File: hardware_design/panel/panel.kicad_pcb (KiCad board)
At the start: 2 copper layers, 60.6 x 128.5 mm, 19 parts

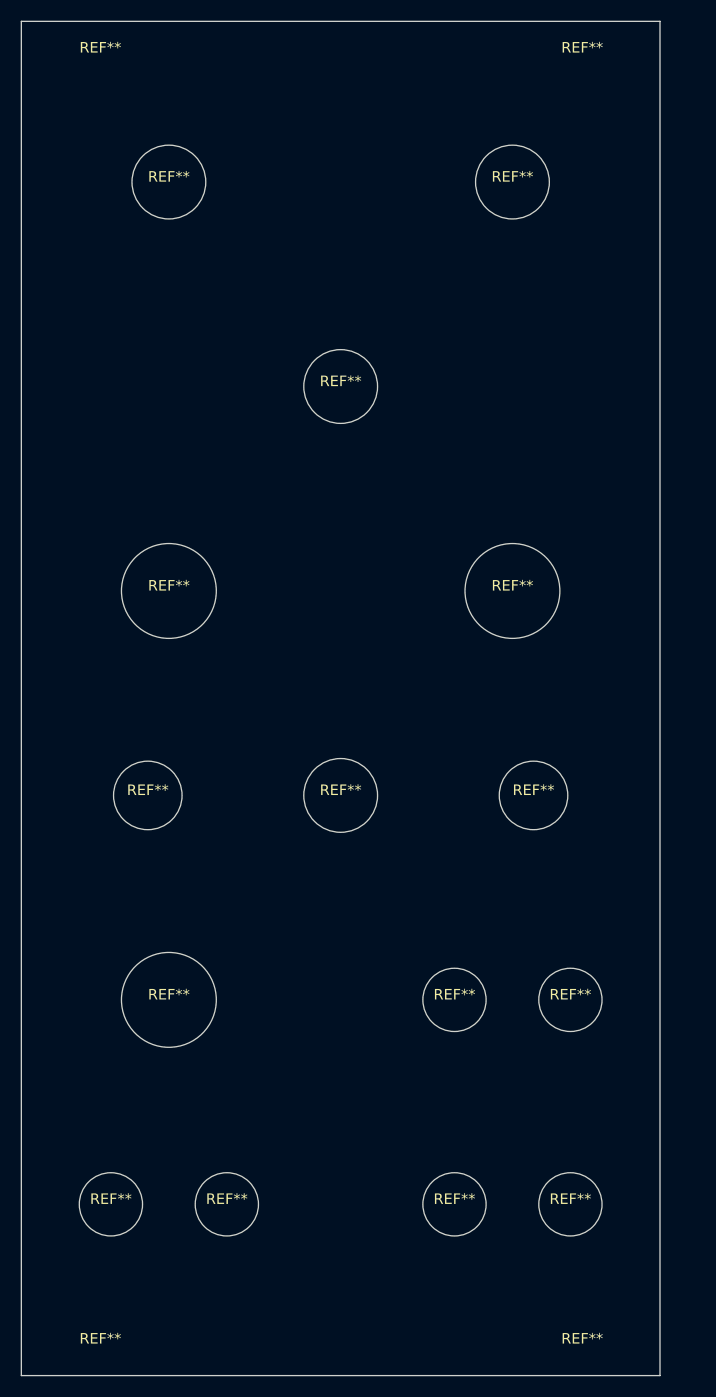
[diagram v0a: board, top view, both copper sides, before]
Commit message: Software switch de-bounce added as a result of Rev 2 testing.
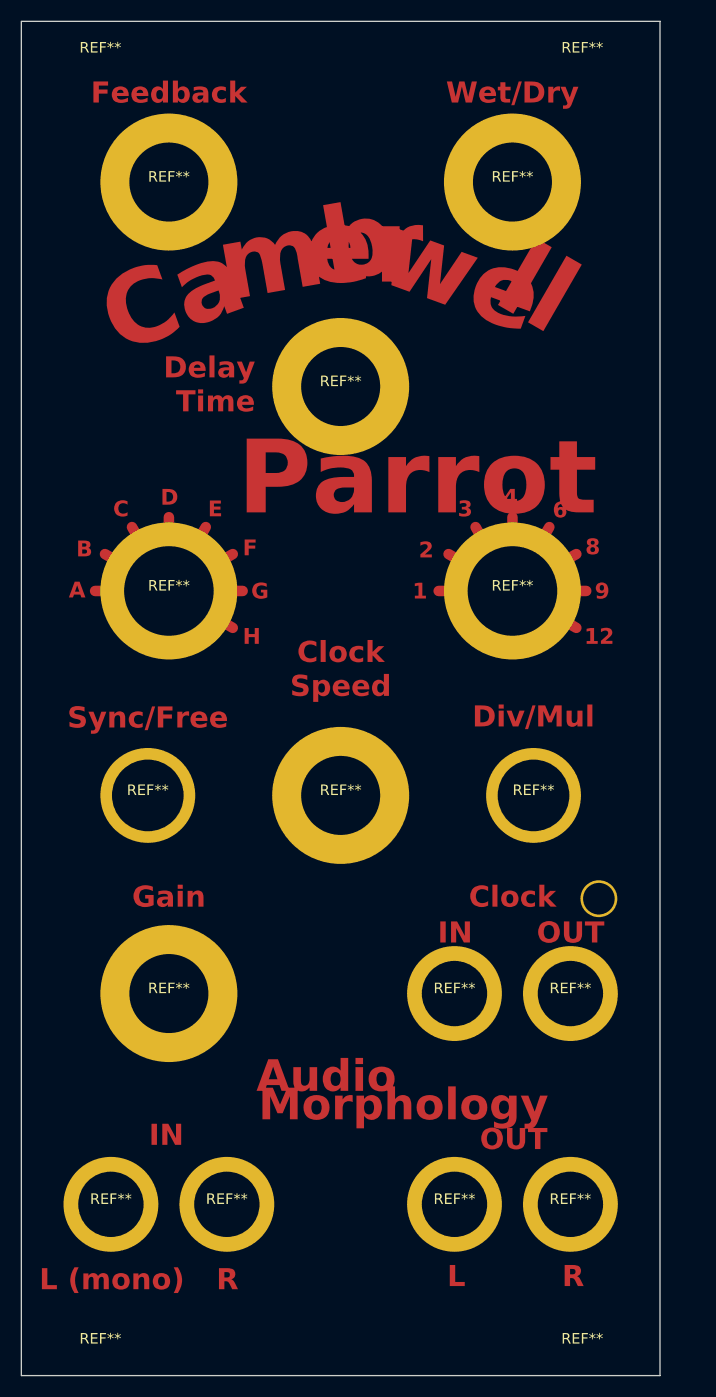
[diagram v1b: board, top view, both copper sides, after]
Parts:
- removed the REF** at (43.0, 36.0)
- removed the REF** at (75.6, 36.0)
- added REF**: NPTH Mechanical 7.5x13, Eurorack:NPTH Mechanical 7.5x13, F.Cu at (75.6, 36.0)
- added REF**: NPTH Mechanical 7.5x13, Eurorack:NPTH Mechanical 7.5x13, F.Cu at (43.0, 36.0)
- added REF**: NPTH Mechanical 3x3.5, Eurorack:NPTH Mechanical 3x3.5, F.Cu at (83.8, 104.0)
- REF** (x6): value NPTH Mechanical 6mm -> NPTH Mechanical 6.2x9; footprint Eurorack:NPTH Mechanical 6mm -> Eurorack:NPTH Mechanical 6.2x9
- REF** (x2): value NPTH Mechanical 9mm -> NPTH Mechanical 8.5x13; footprint Eurorack:NPTH Mechanical 9mm -> Eurorack:NPTH Mechanical 8.5x13
- REF** (x2): value NPTH Mechanical 7mm -> NPTH Mechanical 7.5x13; footprint Eurorack:NPTH Mechanical 7mm -> Eurorack:NPTH Mechanical 7.5x13
- REF** (x2): value NPTH Mechanical 6.5mm -> NPTH Mechanical 6.8x9; footprint Eurorack:NPTH Mechanical 6.5mm -> Eurorack:NPTH Mechanical 6.8x9
- REF**: value NPTH Mechanical 9mm -> NPTH Mechanical 7.5x13; footprint Eurorack:NPTH Mechanical 9mm -> Eurorack:NPTH Mechanical 7.5x13
- moved REF** 0.60 mm to (81.1, 113.0)
- moved REF** 0.60 mm to (70.1, 113.0)
- moved REF** 0.60 mm to (43.0, 113.0)
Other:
- board text added: "1"
- board text added: "12"
- board text added: "2"
- board text added: "3"
- board text added: "4"
- board text added: "6"
- board text added: "8"
- board text added: "9"
- board text added: "A"
- board text added: "Audio"
- board text added: "B"
- board text added: "C"
- board text added: "Ca"
- board text added: "Clock"
- board text added: "Clock Speed"
- board text added: "D"
- board text added: "Delay Time"
- board text added: "Div/Mul"
- board text added: "E"
- board text added: "F"
- board text added: "Feedback"
- board text added: "G"
- board text added: "Gain"
- board text added: "H"
- board text added: "IN"
- board text added: "L"
- board text added: "L (mono)"
- board text added: "Morphology"
- board text added: "OUT"
- board text added: "Parrot"
- board text added: "R"
- board text added: "Sync/Free"
- board text added: "Wet/Dry"
- board text added: "er"
- board text added: "ll"
- board text added: "mb"
- board text added: "we"

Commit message: Rev 2.1 hardware changes
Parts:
- REF** (x2): value NPTH Mechanical 8.5x13 -> NPTH Mechanical 9x13; footprint Eurorack:NPTH Mechanical 8.5x13 -> Eurorack:NPTH Mechanical 9x13
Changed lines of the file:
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@@
 		)
 	)
-	(footprint "Eurorack:NPTH Mechanical 8.5x13"
+	(footprint "Eurorack:NPTH Mechanical 9x13"
 		(layer "F.Cu")
 		(at 43 74.8)
@@
 			)
 		)
-		(property "Value" "NPTH Mechanical 8.5x13"
+		(property "Value" "NPTH Mechanical 9x13"
 			(at 0 1 0)
 			(unlocked yes)
@@
 			)
 		)
-		(property "Footprint" "Eurorack:NPTH Mechanical 8.5x13"
+		(property "Footprint" "Eurorack:NPTH Mechanical 9x13"
 			(at 0 0 0)
 			(unlocked yes)
@@
 			(at 0 0)
 			(size 13 13)
-			(drill 8.5)
+			(drill 9)
 			(layers "F.Cu" "F.Mask")
 		)
@@
 		)
 	)
-	(footprint "Eurorack:NPTH Mechanical 8.5x13"
+	(footprint "Eurorack:NPTH Mechanical 9x13"
 		(layer "F.Cu")
 		(at 75.6 74.8)
@@
 			)
 		)
-		(property "Value" "NPTH Mechanical 8.5x13"
+		(property "Value" "NPTH Mechanical 9x13"
 			(at 0 1 0)
 			(unlocked yes)
@@
 			)
 		)
-		(property "Footprint" "Eurorack:NPTH Mechanical 8.5x13"
+		(property "Footprint" "Eurorack:NPTH Mechanical 9x13"
 			(at 0 0 0)
 			(unlocked yes)
@@
 			(at 0 0)
 			(size 13 13)
-			(drill 8.5)
+			(drill 9)
 			(layers "F.Cu" "F.Mask")
 		)
@@
 	)
 	(gr_text "2"
-		(at 66.7 71.8 0)
+		(at 66.7 71.2 0)
 		(layer "F.Cu")
 		(effects
@@
 	)
 	(gr_text "3"
-		(at 70.4 67.9 0)
+		(at 70.1 67.9 0)
 		(layer "F.Cu")
 		(effects
@@
 	)
 	(gr_text "3"
-		(at 70.4 67.9 0)
+		(at 70.1 67.9 0)
 		(layer "F.Mask")
 		(effects
@@
 	)
 	(gr_text "2"
-		(at 66.7 71.8 0)
+		(at 66.7 71.2 0)
 		(layer "F.Mask")
 		(effects
